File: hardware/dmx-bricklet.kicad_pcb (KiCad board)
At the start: 2 copper layers, 50 x 60 mm, 43 parts, among them P1 CON-SENSOR2, P2 BOOT, P3 DMXCON_2x3, SW1 TER, U1 XMC1XXX48, U2 DRILL, U3 DRILL, U4 DRILL, U5 DRILL, U6 ADM3485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

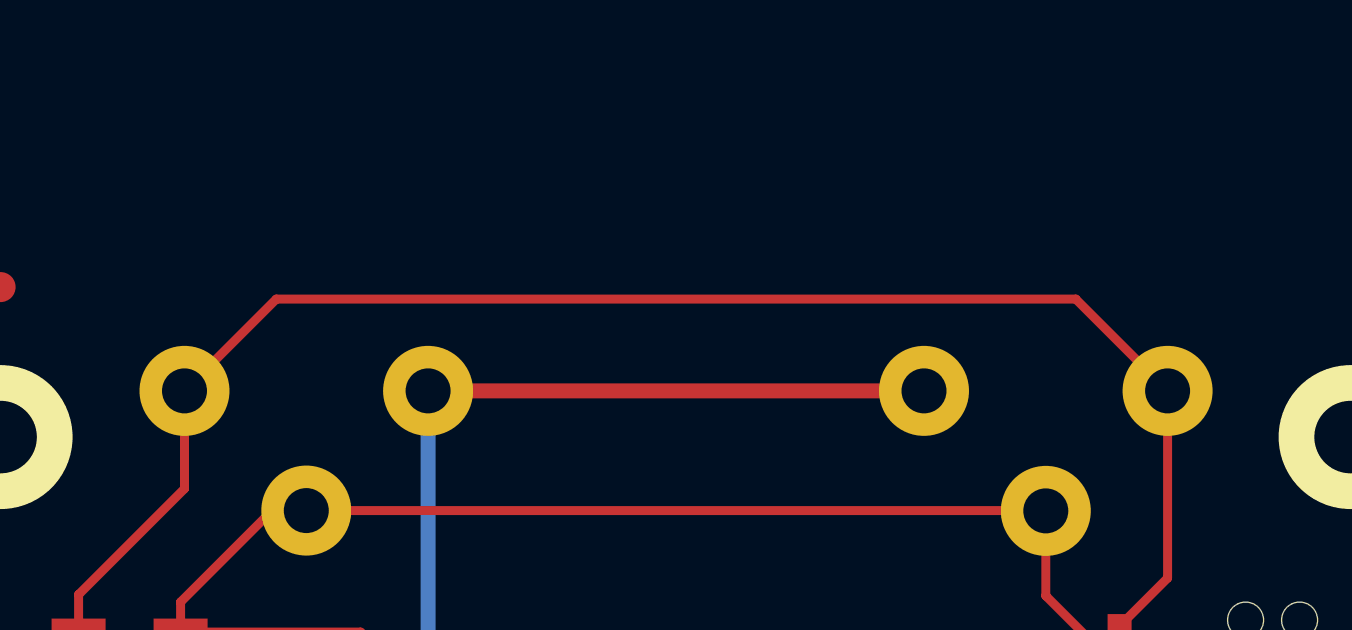
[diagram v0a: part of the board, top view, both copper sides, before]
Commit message: add shielded dmx connector footprint, specify filter
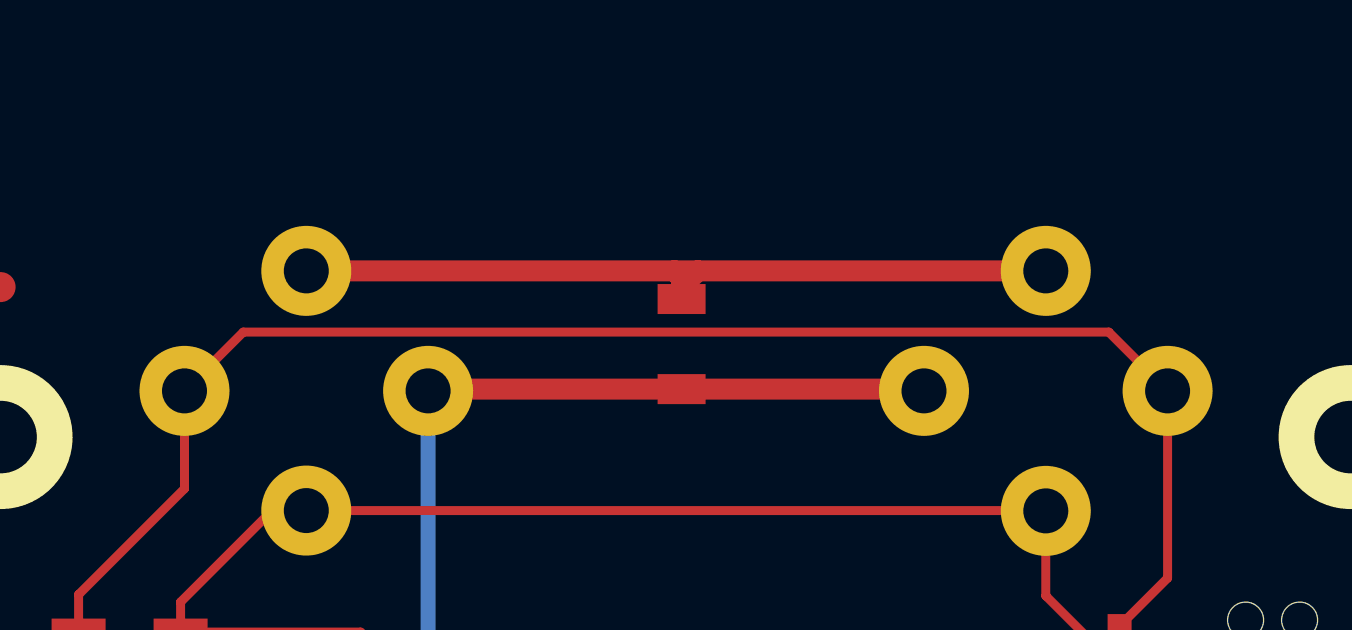
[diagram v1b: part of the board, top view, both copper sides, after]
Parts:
- added R2: DNP, R1206, F.Cu at (148.3, 85.4)
- C10: value TBD -> 220pF
- RP4: value TBD -> 82
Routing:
- net Net-(P3-Pad7): track 0.00 -> 26.9 mm
- net Net-(D5-Pad1): track 70.8 -> 69.9 mm

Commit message: Fix edge cuts; specify R9 to 0Ohm
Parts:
- C1, C2, C3, C4, C5, C6, C8, C9: footprint kicad-libraries:C0603F -> C0603F
- C10: footprint kicad-libraries:C0402E -> C0402E
- C7: footprint kicad-libraries:C0603E -> C0603E
- D1, D2, D3: footprint kicad-libraries:D0603E -> D0603E
- D4, D5: footprint kicad-libraries:DO-214AC -> DO-214AC
- L1: footprint kicad-libraries:WE-SL -> WE-SL
- P1: footprint kicad-libraries:CON-SENSOR2 -> CON-SENSOR2
- P3: footprint kicad-libraries:DMX_IN_OUT_2x3POL -> DMX_IN_OUT_2x3POL
- R1: footprint kicad-libraries:R0603 -> R0603F
- R3, R4, R5: footprint kicad-libraries:R0603F -> R0603F
- R9: value TBD -> 0; footprint kicad-libraries:R0402E -> R0402E
- RP4: footprint kicad-libraries:4X0402 -> 4X0402
- U2, U3, U4, U5: footprint kicad-libraries:DRILL_NP -> DRILL_NP
- U6: footprint kicad-libraries:SOIC8 -> SOIC8
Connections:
- P1 pad 1: (no net) -> Net-(P1-Pad1)
- RP1 pad 1: (no net) -> Net-(RP1-Pad1)
- RP1 pad 8: (no net) -> Net-(RP1-Pad8)
- SW1 pad 3: (no net) -> Net-(SW1-Pad3)
- SW1 pad 4: (no net) -> Net-(SW1-Pad4)
- SW1 pad 5: (no net) -> Net-(SW1-Pad5)
- SW1 pad 6: (no net) -> Net-(SW1-Pad6)
- U1 pad 10: (no net) -> Net-(U1-Pad10)
- U1 pad 11: (no net) -> Net-(U1-Pad11)
- U1 pad 12: (no net) -> Net-(U1-Pad12)
- U1 pad 16: (no net) -> Net-(U1-Pad16)
- U1 pad 2: (no net) -> Net-(U1-Pad2)
- U1 pad 21: (no net) -> Net-(U1-Pad21)
- U1 pad 22: (no net) -> Net-(U1-Pad22)
- U1 pad 26: (no net) -> Net-(U1-Pad26)
- U1 pad 29: (no net) -> Net-(U1-Pad29)
- U1 pad 3: (no net) -> Net-(U1-Pad3)
- U1 pad 30: (no net) -> Net-(U1-Pad30)
- U1 pad 31: (no net) -> Net-(U1-Pad31)
- U1 pad 32: (no net) -> Net-(U1-Pad32)
- U1 pad 33: (no net) -> Net-(U1-Pad33)
- U1 pad 34: (no net) -> Net-(U1-Pad34)
- U1 pad 35: (no net) -> Net-(U1-Pad35)
- U1 pad 36: (no net) -> Net-(U1-Pad36)
- U1 pad 39: (no net) -> Net-(U1-Pad39)
- U1 pad 4: (no net) -> Net-(U1-Pad4)
- U1 pad 40: (no net) -> Net-(U1-Pad40)
- U1 pad 43: (no net) -> Net-(U1-Pad43)
- U1 pad 44: (no net) -> Net-(U1-Pad44)
- U1 pad 45: (no net) -> Net-(U1-Pad45)
- U1 pad 5: (no net) -> Net-(U1-Pad5)
- U1 pad 6: (no net) -> Net-(U1-Pad6)
- U1 pad 7: (no net) -> Net-(U1-Pad7)
- U1 pad 8: (no net) -> Net-(U1-Pad8)
- U1 pad 9: (no net) -> Net-(U1-Pad9)
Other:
- board size 50 x 60 mm -> 50 x 55 mm

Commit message: Fix LED colors in 3d model
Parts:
- P3: footprint DMX_IN_OUT_2x3POL -> kicad-libraries:DMX_IN_OUT_2x3POL

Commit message: add termination switch silkscreen description
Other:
- board text added: "Termination No Termination"
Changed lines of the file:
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@@
-(kicad_pcb (version 4) (host pcbnew 4.0.2+dfsg1-stable)
+(kicad_pcb (version 4) (host pcbnew 4.0.7-e2-6376~58~ubuntu17.04.1)
   (general
     (links 91)
     (no_connects 1)
-    (area 123.009999 65.929999 173.210001 121.130001)
+    (area 122.255139 57.03014 173.964861 121.884861)
     (thickness 1.6002)
-    (drawings 13)
+    (drawings 14)
     (tracks 384)
     (zones 0)
@@
     )
   )
+  (gr_text "Termination\n\n\n\nNo Termination" (at 162.11 98.03) (layer F.SilkS)
+    (effects (font (size 0.75 0.75) (thickness 0.15)) (justify right))
+  )
   (gr_arc (start 170.61 68.53) (end 170.61 66.03) (angle 90) (layer Edge.Cuts) (width 0.2))
